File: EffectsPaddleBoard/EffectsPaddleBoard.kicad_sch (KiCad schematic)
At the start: 1 part, among them J1 USB_C_Receptacle_USB2.0

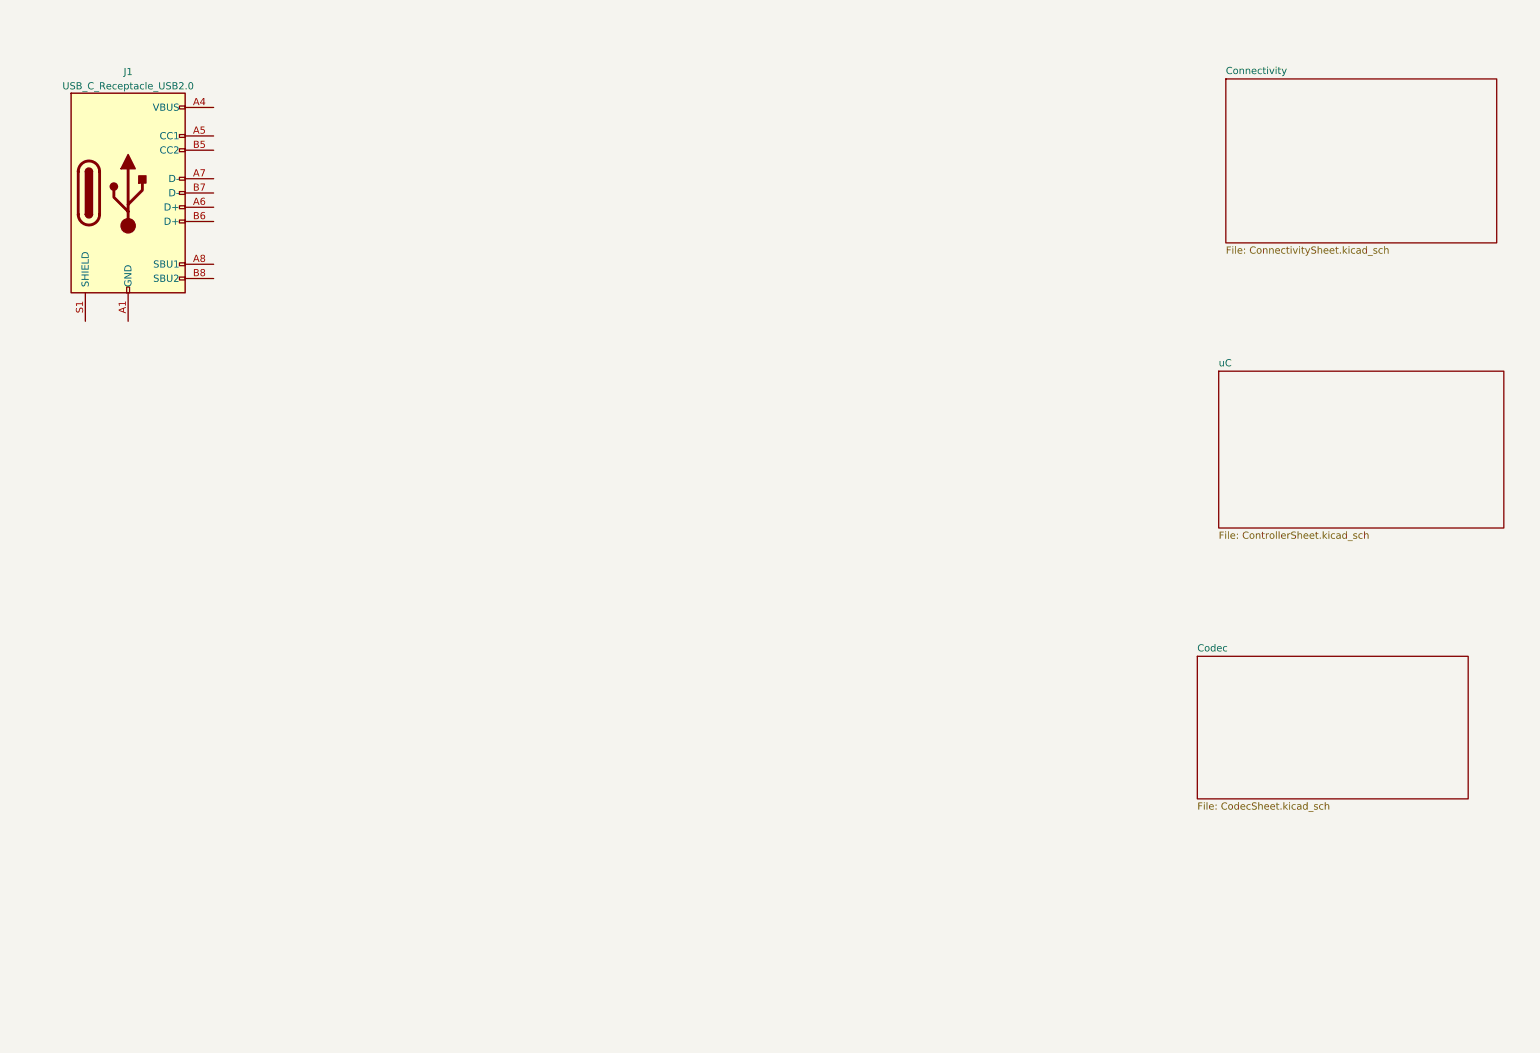
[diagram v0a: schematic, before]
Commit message: Added power to uC, but overall power not finished
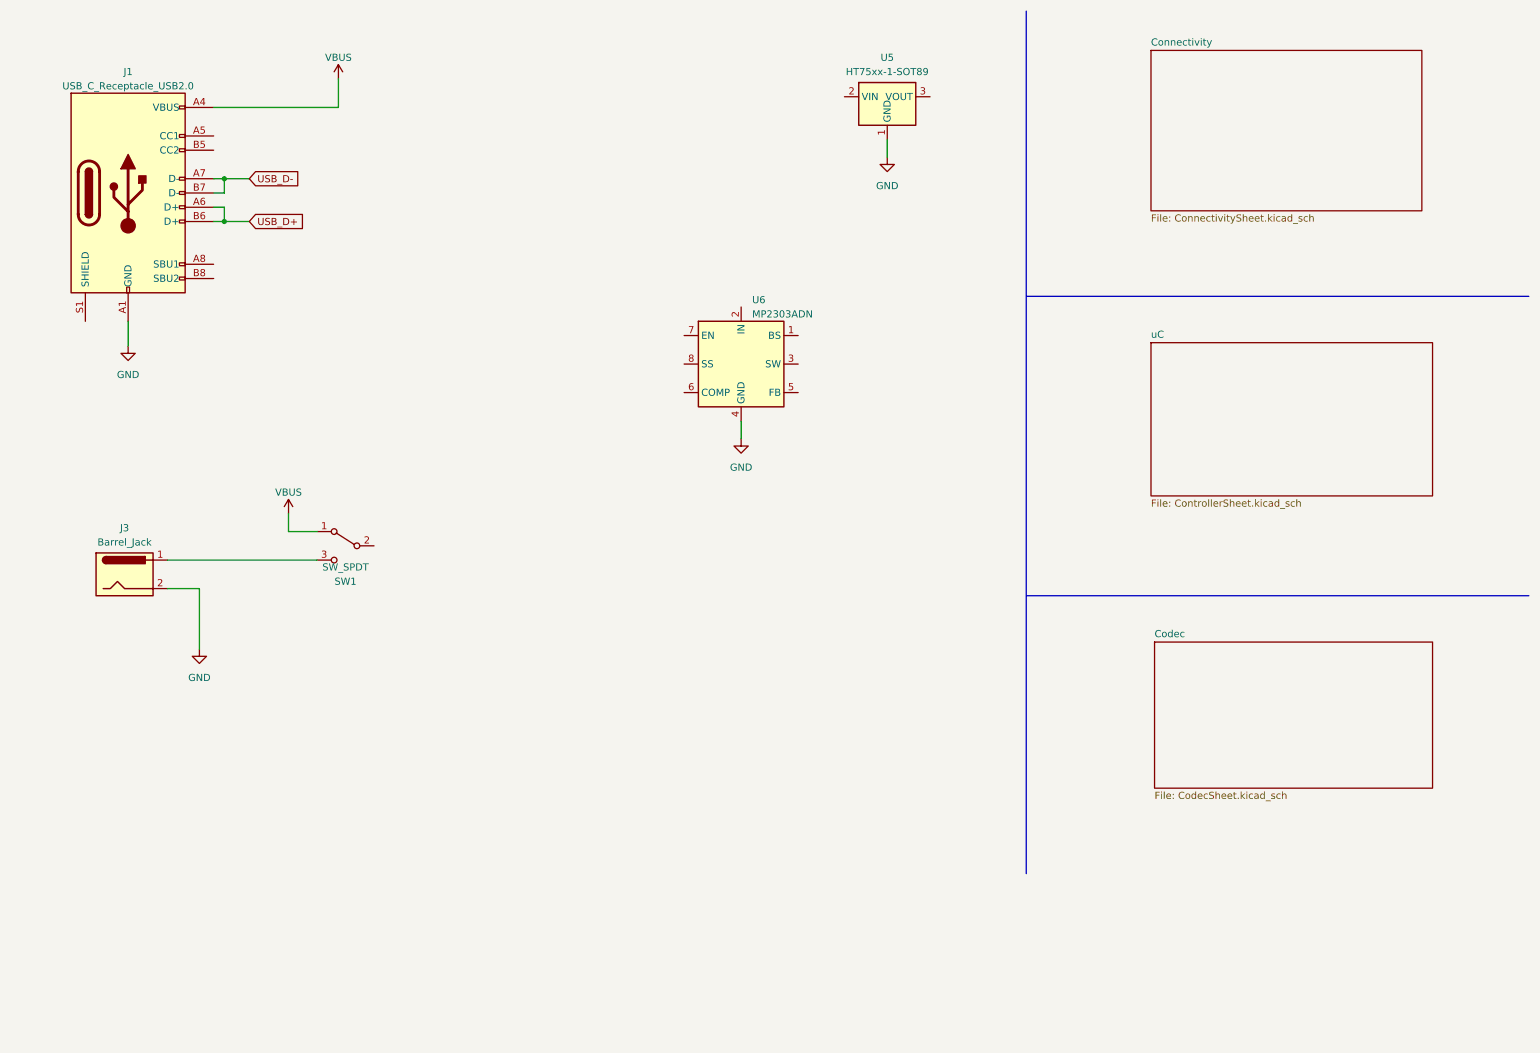
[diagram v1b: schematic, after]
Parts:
- added J3: Barrel_Jack, symbol Connector:Barrel_Jack
- added SW1: SW_SPDT, symbol Switch:SW_SPDT
- added U5: HT75xx-1-SOT89, Package_TO_SOT_SMD:SOT-89-3, symbol Regulator_Linear:HT75xx-1-SOT89
- added U6: MP2303ADN, Package_SO:SOIC-8-1EP_3.9x4.9mm_P1.27mm_EP2.62x3.51mm, symbol Regulator_Switching:MP2303ADN
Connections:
- net GND: now reaches J1.A1 (GND), J1.A12 (GND), J1.B1 (GND), J1.B12 (GND)
- net GND: now also J3.2, U5.1 (GND), U6.4 (GND)
- net VBUS: now reaches J1.A4 (VBUS), J1.A9 (VBUS), J1.B4 (VBUS), J1.B9 (VBUS)
- net VBUS: now also SW1.1 (A)
- net USB_D+: now reaches J1.A6 (D+)
- net USB_D+: now also J1.B6 (D+)
- net USB_D-: now reaches J1.A7 (D-)
- net USB_D-: now also J1.B7 (D-)
- new net: J3.1, SW1.3 (C)
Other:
- company: (none) -> Selbstständig
- title: (none) -> Effects Paddle

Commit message: While wiring the codec, I found that I used the wrong controller and so I2S communication is unidirectional only: TODO: fix that
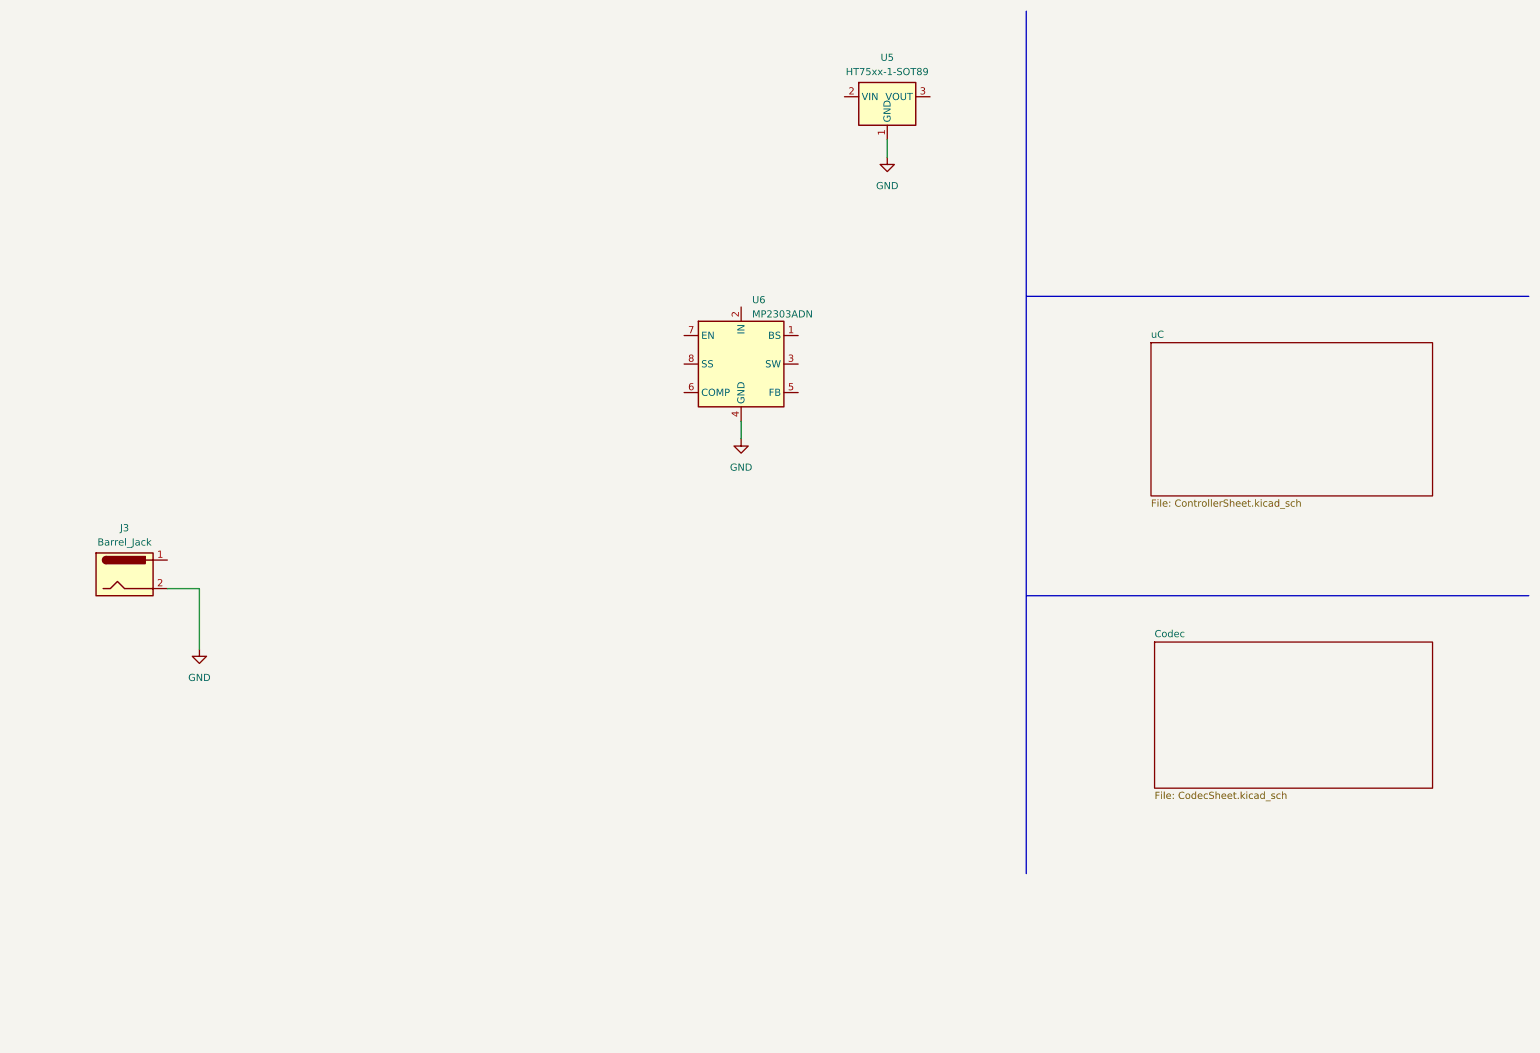
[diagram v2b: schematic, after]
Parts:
- removed J1: USB_C_Receptacle_USB2.0, symbol Connector:USB_C_Receptacle_USB2.0
- removed SW1: SW_SPDT, symbol Switch:SW_SPDT
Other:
- removed sheet Connectivity

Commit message: Added power supply
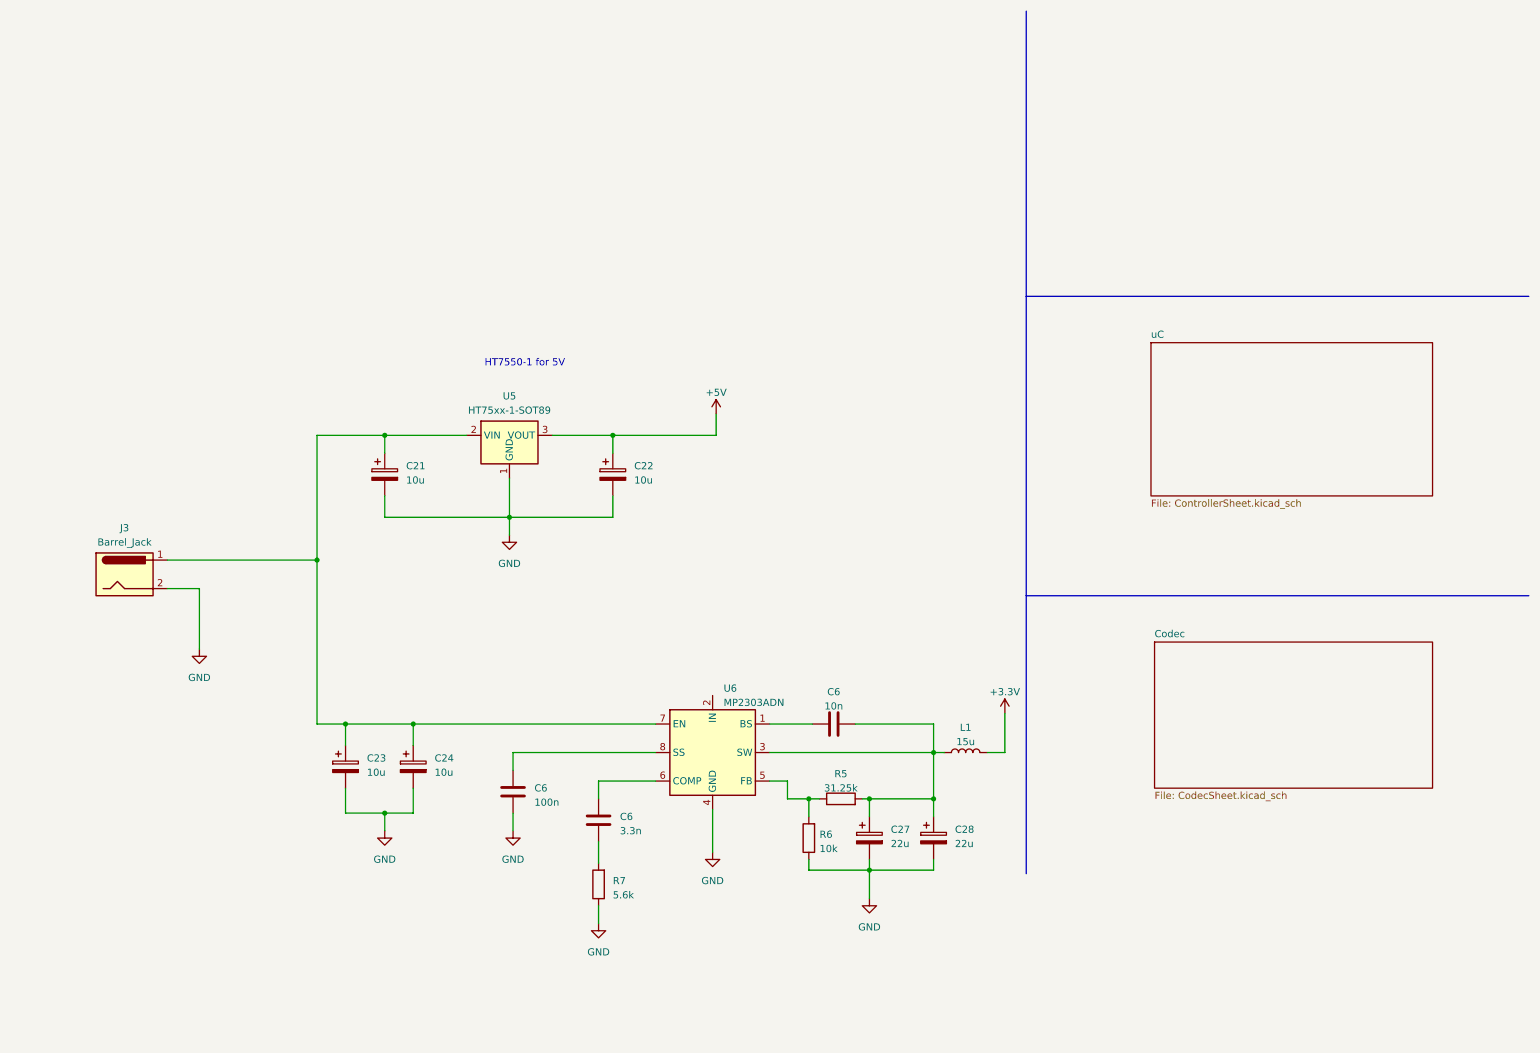
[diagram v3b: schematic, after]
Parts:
- added C21, C22, C23, C24: 10u, symbol Device:C_Polarized
- added C27, C28: 22u, symbol Device:C_Polarized
- added C6: 3.3n, symbol Device:C
- added C6: 10n, symbol Device:C
- added C6: 100n, symbol Device:C
- added L1: 15u, symbol Device:L
- added R5: 31.25k, symbol Device:R
- added R6: 10k, symbol Device:R
- added R7: 5.6k, symbol Device:R
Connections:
- net GND: now also C21.2, C22.2, C23.2, C24.2, C27.2, C28.2, C6.2, R6.1, R7.1
- net at U5.2 (VIN): now also J3.1, U6.7 (EN), C21.1, C23.1, C24.1
- net +5V: now reaches U5.3 (VOUT)
- net +5V: now also C22.1
- net at U6.1 (BS): now also C6.1
- net at U6.3 (SW): now also C27.1, C28.1, C6.2, L1.1, R5.2
- net at U6.5 (FB): now also R5.1, R6.2
- net at U6.6 (COMP): now also C6.1
- net at U6.8 (SS): now also C6.1
- new net: C6.2, R7.2
- new net +3.3V: L1.2
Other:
- note added: "HT7550-1 for 5V"
- moved on the sheet: U5, U6

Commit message: Finished schematic
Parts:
- removed C21, C22, C23: 10u, symbol Device:C_Polarized
- removed C27, C28: 22u, symbol Device:C_Polarized
- removed C6: 3.3n, symbol Device:C
- removed C6: 10n, symbol Device:C
- removed C6: 100n, symbol Device:C
- removed L1: 15u, symbol Device:L
- removed R5: 31.25k, symbol Device:R
- removed R6: 10k, symbol Device:R
- removed R7: 5.6k, symbol Device:R
- removed U5: HT75xx-1-SOT89, Package_TO_SOT_SMD:SOT-89-3, symbol Regulator_Linear:HT75xx-1-SOT89
- removed U6: MP2303ADN, Package_SO:SOIC-8-1EP_3.9x4.9mm_P1.27mm_EP2.62x3.51mm, symbol Regulator_Switching:MP2303ADN
- added C21, C27: 10u, symbol Device:C_Small
- added C22, C37: 15n, symbol Device:C_Small
- added C23, C38: 100n, symbol Device:C_Small
- added C25, C26, C28, C29: 220p, symbol Device:C_Small
- added C30 (x2), C31 (x2): 1u, symbol Device:C
- added C32 (x2): 10u, symbol Device:C
- added C39, C40: 470u, symbol Device:C_Polarized
- added D2, D3: B230, Diode_SMD:D_SMB, symbol Diode:B230
- added FB1 (x2): 600, symbol Device:FerriteBead
- added L1, L2: 15u, symbol Device:L_Small
- added R10, R5: 332k, symbol Device:R_Small
- added R11, R6: 68.1k, symbol Device:R_Small
- added R12, R9: 30.9k, symbol Device:R_Small
- added R13: 10k, symbol Device:R_Small
- added R14, R15: 3.9k, symbol Device:R_Small
- added R21: 4k7, symbol Device:R_Small
- added R22: 3k9, symbol Device:R_Small
- added R7: 10.2k, symbol Device:R_Small
- added R8: 3.24k, symbol Device:R_Small
- added TP1, TP2: TestPoint, symbol Connector:TestPoint
- added U2, U4: TPS54233, Package_SO:SOIC-8_3.9x4.9mm_P1.27mm, symbol Regulator_Switching:TPS54233
- C24: value 10u -> 470u
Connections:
- net +3.3V: now also C24.1, C30.1, FB1.2, L1.2, R22.1, R7.1, TP1.1
- net +5V: now also C30.1, C39.1, FB1.2, L2.2, R13.1, TP2.1
- net GND: now also C21.2, C22.2, C25.2, C27.2, C29.2, C30.2, C30.2, C31.2, C31.2, C32.2, C32.2, C37.2, C39.2, C40.2, D2.2 (A), D3.2 (A), R11.2, R12.2, R14.2, R15.2, R21.2, R6.2, R8.2, R9.2, U2.7 (GND), U4.7 (GND)
- net at J3.1: now also C21.1, C27.1, R10.1, R5.1, U2.2 (VIN), U4.2 (VIN); no longer C24.1
- new net: C23.2, D2.1 (K), L1.1, U2.8 (PH)
- new net: C28.1, C29.1, U4.6 (COMP)
- new net: R13.2, R14.1, R15.1, U4.5 (FB)
- new net: R5.2, R6.1, U2.3 (EN)
- new net: C28.2, R12.1
- new net: R7.2, R8.1, U2.5 (FB)
- new net: C22.1, U2.4 (SS)
- new net: C38.1, U4.1 (BOOT)
- new net: R10.2, R11.1, U4.3 (EN)
- new net: C37.1, U4.4 (SS)
- new net: C38.2, D3.1 (K), L2.1, U4.8 (PH)
- new net: C26.2, R9.1
- new net: C23.1, U2.1 (BOOT)
- new net: C25.1, C26.1, U2.6 (COMP)
- new net +1V8: C40.1, R21.1, R22.2
- new net +3.3VA: C31.1, C32.1, FB1.1
- new net +5VA: C31.1, C32.1, FB1.1
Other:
- added sheet Analog_FrontBackend (AFB.kicad_sch)
- note removed: "HT7550-1 for 5V"

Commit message: Began with pcb layout
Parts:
- added TP3, TP4: TestPoint, Connector_Pin:Pin_D1.3mm_L11.0mm, symbol Connector:TestPoint
- C21, C27, C30, C31, C32: footprint (none) -> Capacitor_SMD:C_1206_3216Metric
- C22, C23, C25, C26, C28, C29, C37, C38: footprint (none) -> Capacitor_SMD:C_0402_1005Metric
- C24, C39, C40: footprint (none) -> Capacitor_SMD:CP_Elec_8x10
- FB1, L1, L2: footprint (none) -> Inductor_SMD:L_0603_1608Metric
- J3: footprint (none) -> Connector_BarrelJack:BarrelJack_SwitchcraftConxall_RAPC10U_Horizontal
- R10, R11, R12, R13, R14, R15, R21, R22, R5, R6, R7, R8, R9: footprint (none) -> Resistor_SMD:R_1206_3216Metric
- TP1, TP2: footprint (none) -> Connector_Pin:Pin_D1.3mm_L11.0mm
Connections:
- net GND: now also TP3.1, TP4.1

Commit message: Reviev by David and netnaming
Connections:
- net ph3v3out: now reaches C23.2, D2.1 (K), L1.1, U2.8 (PH)
- net comp5v: now reaches C28.1, C29.1, U4.6 (COMP)
- net fb5v: now reaches R13.2, R14.1, R15.1, U4.5 (FB)
- net en3v3: now reaches R5.2, R6.1, U2.3 (EN)
- net Barreljack_in: now reaches C21.1, C27.1, J3.1, R10.1, R5.1, U2.2 (VIN), U4.2 (VIN)
- net fb3v3: now reaches R7.2, R8.1, U2.5 (FB)
- net b5v: now reaches C38.1, U4.1 (BOOT)
- net en5v: now reaches R10.2, R11.1, U4.3 (EN)
- net ph5vout: now reaches C38.2, D3.1 (K), L2.1, U4.8 (PH)
- net b3v3: now reaches C23.1, U2.1 (BOOT)
- net comp3v3: now reaches C25.1, C26.1, U2.6 (COMP)
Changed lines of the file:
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@@
     (stroke (width 0) (type default))
+  )
+  (label "comp3v3" (at 107.95 132.715 90) (fields_autoplaced)
+    (effects (font (size 1.27 1.27)) (justify left bottom))
+  )
+  (label "fb5v" (at 155.575 60.325 0) (fields_autoplaced)
+    (effects (font (size 1.27 1.27)) (justify left bottom))
+  )
+  (label "en5v" (at 100.33 39.37 0) (fields_autoplaced)
+    (effects (font (size 1.27 1.27)) (justify left bottom))
+  )
+  (label "b3v3" (at 139.7 109.855 0) (fields_autoplaced)
+    (effects (font (size 1.27 1.27)) (justify left bottom))
+  )
+  (label "fb3v3" (at 163.83 135.89 0) (fields_autoplaced)
+    (effects (font (size 1.27 1.27)) (justify left bottom))
+  )
+  (label "comp5v" (at 100.33 54.61 90) (fields_autoplaced)
+    (effects (font (size 1.27 1.27)) (justify left bottom))
+  )
+  (label "Barreljack_in" (at 62.23 109.855 0) (fields_autoplaced)
+    (effects (font (size 1.27 1.27)) (justify left bottom))
+  )
+  (label "ph5vout" (at 135.89 39.37 0) (fields_autoplaced)
+    (effects (font (size 1.27 1.27)) (justify left bottom))
+  )
+  (label "b5v" (at 132.715 34.29 0) (fields_autoplaced)
+    (effects (font (size 1.27 1.27)) (justify left bottom))
+  )
+  (label "en3v3" (at 106.045 114.935 0) (fields_autoplaced)
+    (effects (font (size 1.27 1.27)) (justify left bottom))
+  )
+  (label "ph3v3out" (at 141.605 114.935 0) (fields_autoplaced)
+    (effects (font (size 1.27 1.27)) (justify left bottom))
   )
   (symbol (lib_id "power:+5V") (at 100.965 165.1 0) (unit 1)
